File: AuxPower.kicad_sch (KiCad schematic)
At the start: 9 parts, among them U1 I6A4W020A033V-003-R

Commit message: Cleaning up for prototype run
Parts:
- added J1: Conn_01x02_Female, Connector_JST:JST_XH_B2B-XH-A_1x02_P2.50mm_Vertical, symbol Connector:Conn_01x02_Female
- RV1: MFN# (none) -> 3266W-1-503LF
- U1: MFN# (none) -> I6A24014A033V-003-R
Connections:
- net +9V: now also J1.1 (Pin_1)
- net GND: now also J1.2 (Pin_2)
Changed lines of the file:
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@@
   (junction (at 96.52 48.26) (diameter 0) (color 0 0 0 0)
   )
+  (junction (at 114.3 48.26) (diameter 0) (color 0 0 0 0)
+  )
   (junction (at 91.44 73.66) (diameter 0) (color 0 0 0 0)
   )
   (junction (at 101.6 55.88) (diameter 0) (color 0 0 0 0)
+  )
+  (junction (at 110.49 55.88) (diameter 0) (color 0 0 0 0)
   )
   (junction (at 26.67 55.88) (diameter 0) (color 0 0 0 0)
@@
     (stroke (width 0) (type default) (color 0 0 0 0))
   )
+  (wire (pts (xy 121.92 55.88) (xy 110.49 55.88))
+    (stroke (width 0) (type default) (color 0 0 0 0))
+  )
   (wire (pts (xy 101.6 55.88) (xy 110.49 55.88))
     (stroke (width 0) (type default) (color 0 0 0 0))
@@
     (stroke (width 0) (type default) (color 0 0 0 0))
   )
+  (wire (pts (xy 121.92 50.8) (xy 121.92 55.88))
+    (stroke (width 0) (type default) (color 0 0 0 0))
+  )
   (wire (pts (xy 52.07 53.34) (xy 52.07 48.26))
     (stroke (width 0) (type default) (color 0 0 0 0))
   )
   (wire (pts (xy 54.61 53.34) (xy 52.07 53.34))
+    (stroke (width 0) (type default) (color 0 0 0 0))
+  )
+  (wire (pts (xy 114.3 48.26) (xy 121.92 48.26))
     (stroke (width 0) (type default) (color 0 0 0 0))
   )
@@
     )
     (property "Datasheet" "~" (id 3) (at 45.72 53.34 0)
+      (effects (font (size 1.27 1.27)) hide)
+    )
+    (pin "1")
+    (pin "2")
+  )
+  (symbol (lib_id "Connector:Conn_01x02_Female") (at 127 48.26 0) (unit 1)
+    (in_bom yes) (on_board yes) (fields_autoplaced)
+    (property "Reference" "J1" (id 0) (at 128.27 49.5299 0)
+      (effects (font (size 1.27 1.27)) (justify left))
+    )
+    (property "Value" "Conn_01x02_Female" (id 1) (at 128.27 50.7999 0)
+      (effects (font (size 1.27 1.27)) (justify left) hide)
+    )
+    (property "Footprint" "Connector_JST:JST_XH_B2B-XH-A_1x02_P2.50mm_Vertical" (id 2) (at 127 48.26 0)
+      (effects (font (size 1.27 1.27)) hide)
+    )
+    (property "Datasheet" "~" (id 3) (at 127 48.26 0)
       (effects (font (size 1.27 1.27)) hide)
     )
@@
       (effects (font (size 1.27 1.27)) hide)
     )
-    (property "Datasheet" "~" (id 3) (at 97.79 73.66 0)
+    (property "Datasheet" "" (id 3) (at 97.79 73.66 0)
+      (effects (font (size 1.27 1.27)) hide)
+    )
+    (property "MFN#" "3266W-1-503LF" (id 4) (at 97.79 73.66 90)
       (effects (font (size 1.27 1.27)) hide)
     )
@@
       (effects (font (size 1.27 1.27)) hide)
     )
+    (property "MFN#" "I6A24014A033V-003-R" (id 4) (at 81.28 58.42 0)
+      (effects (font (size 1.27 1.27)) hide)
+    )

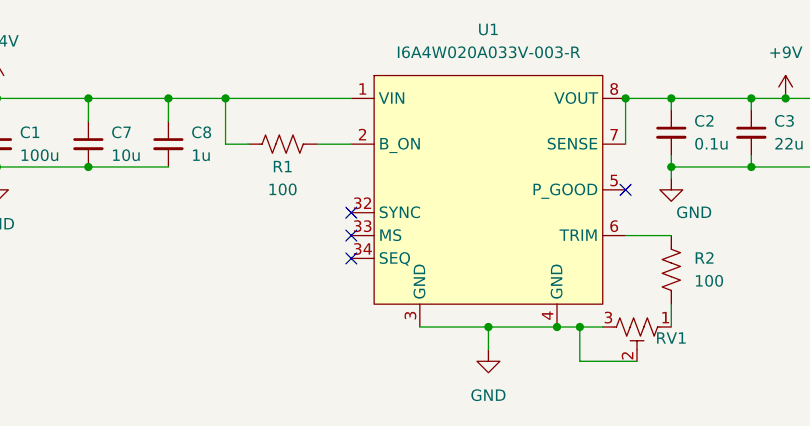
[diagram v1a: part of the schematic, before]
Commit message: No point using Fuses w/o fuse holders, Also added 3D models
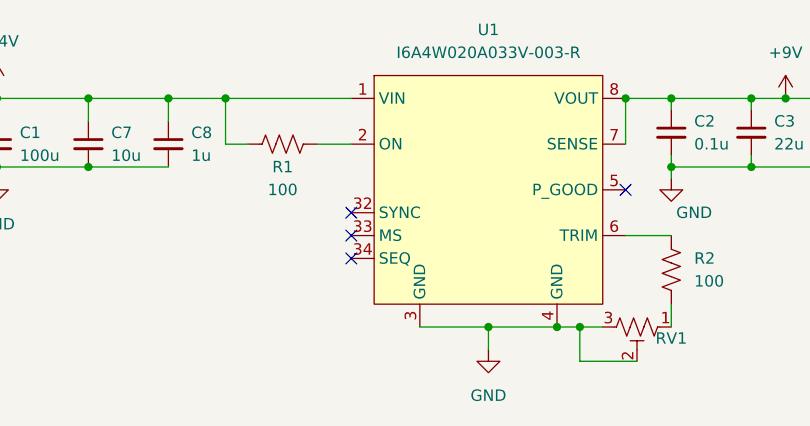
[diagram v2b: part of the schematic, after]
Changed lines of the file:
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@@
       (effects (font (size 1.27 1.27)) hide)
     )
+    (pin "1")
     (pin "2")
-    (pin "1")
     (pin "3")
     (pin "32")

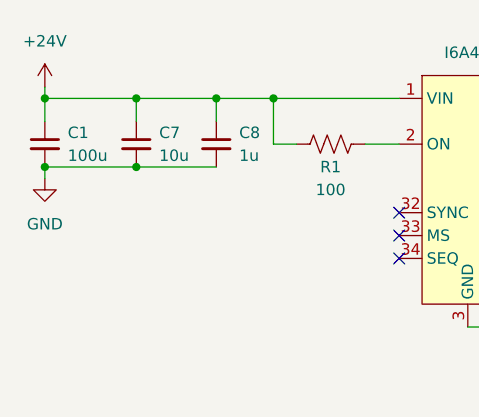
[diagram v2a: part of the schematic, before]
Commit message: Added BOM and updated Cap footprint according to availability
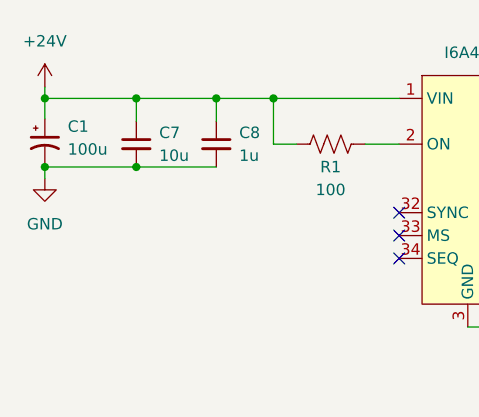
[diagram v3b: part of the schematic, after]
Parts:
- removed C1: 100u, Capacitor_SMD:C_0603_1608Metric, symbol Device:C_Small
- added C1: 100u, Capacitor_SMD:CP_Elec_10x10, symbol Device:C_Polarized_Small_US
- C3: footprint Capacitor_SMD:C_0603_1608Metric -> Capacitor_Tantalum_SMD:CP_EIA-7343-15_Kemet-W
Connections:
- net +24V: now also C1.1
- net GND: now also C1.2
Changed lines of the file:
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@@
   (junction (at 110.49 55.88) (diameter 0) (color 0 0 0 0)
   )
+  (junction (at 36.83 55.88) (diameter 0) (color 0 0 0 0)
+  )
+  (junction (at 26.67 48.26) (diameter 0) (color 0 0 0 0)
+  )
+  (junction (at 110.49 48.26) (diameter 0) (color 0 0 0 0)
+  )
+  (junction (at 36.83 48.26) (diameter 0) (color 0 0 0 0)
+  )
+  (junction (at 88.9 73.66) (diameter 0) (color 0 0 0 0)
+  )
+  (junction (at 81.28 73.66) (diameter 0) (color 0 0 0 0)
+  )
+  (junction (at 101.6 48.26) (diameter 0) (color 0 0 0 0)
+  )
+  (junction (at 52.07 48.26) (diameter 0) (color 0 0 0 0)
+  )
   (junction (at 26.67 55.88) (diameter 0) (color 0 0 0 0)
-  )
-  (junction (at 36.83 55.88) (diameter 0) (color 0 0 0 0)
-  )
-  (junction (at 26.67 48.26) (diameter 0) (color 0 0 0 0)
-  )
-  (junction (at 110.49 48.26) (diameter 0) (color 0 0 0 0)
-  )
-  (junction (at 36.83 48.26) (diameter 0) (color 0 0 0 0)
-  )
-  (junction (at 88.9 73.66) (diameter 0) (color 0 0 0 0)
-  )
-  (junction (at 81.28 73.66) (diameter 0) (color 0 0 0 0)
-  )
-  (junction (at 101.6 48.26) (diameter 0) (color 0 0 0 0)
-  )
-  (junction (at 52.07 48.26) (diameter 0) (color 0 0 0 0)
   )
   (junction (at 45.72 48.26) (diameter 0) (color 0 0 0 0)
@@
     (stroke (width 0) (type default) (color 0 0 0 0))
   )
-  (wire (pts (xy 26.67 48.26) (xy 26.67 50.8))
+  (wire (pts (xy 26.67 48.26) (xy 26.67 50.546))
+    (stroke (width 0) (type default) (color 0 0 0 0))
+  )
+  (wire (pts (xy 26.67 55.626) (xy 26.67 55.88))
+    (stroke (width 0) (type default) (color 0 0 0 0))
+  )
+  (wire (pts (xy 101.6 48.26) (xy 101.6 49.53))
+    (stroke (width 0) (type default) (color 0 0 0 0))
+  )
+  (wire (pts (xy 96.52 63.5) (xy 101.6 63.5))
+    (stroke (width 0) (type default) (color 0 0 0 0))
+  )
+  (wire (pts (xy 45.72 48.26) (xy 52.07 48.26))
+    (stroke (width 0) (type default) (color 0 0 0 0))
+  )
+  (wire (pts (xy 121.92 55.88) (xy 110.49 55.88))
+    (stroke (width 0) (type default) (color 0 0 0 0))
+  )
+  (wire (pts (xy 101.6 55.88) (xy 110.49 55.88))
+    (stroke (width 0) (type default) (color 0 0 0 0))
+  )
+  (wire (pts (xy 26.67 55.88) (xy 36.83 55.88))
+    (stroke (width 0) (type default) (color 0 0 0 0))
+  )
+  (wire (pts (xy 36.83 48.26) (xy 45.72 48.26))
+    (stroke (width 0) (type default) (color 0 0 0 0))
+  )
+  (wire (pts (xy 101.6 48.26) (xy 110.49 48.26))
+    (stroke (width 0) (type default) (color 0 0 0 0))
+  )
+  (wire (pts (xy 66.04 53.34) (xy 62.23 53.34))
+    (stroke (width 0) (type default) (color 0 0 0 0))
+  )
+  (wire (pts (xy 52.07 48.26) (xy 66.04 48.26))
+    (stroke (width 0) (type default) (color 0 0 0 0))
+  )
+  (wire (pts (xy 101.6 57.15) (xy 101.6 55.88))
+    (stroke (width 0) (type default) (color 0 0 0 0))
+  )
+  (wire (pts (xy 91.44 73.66) (xy 93.98 73.66))
+    (stroke (width 0) (type default) (color 0 0 0 0))
+  )
+  (wire (pts (xy 121.92 50.8) (xy 121.92 55.88))
+    (stroke (width 0) (type default) (color 0 0 0 0))
+  )
+  (wire (pts (xy 52.07 53.34) (xy 52.07 48.26))
+    (stroke (width 0) (type default) (color 0 0 0 0))
+  )
+  (wire (pts (xy 54.61 53.34) (xy 52.07 53.34))
     (stroke (width 0) (type default) (color 0 0 0 0))
   )
   (wire (pts (xy 26.67 55.88) (xy 26.67 57.15))
-    (stroke (width 0) (type default) (color 0 0 0 0))
-  )
-  (wire (pts (xy 101.6 48.26) (xy 101.6 49.53))
-    (stroke (width 0) (type default) (color 0 0 0 0))
-  )
-  (wire (pts (xy 96.52 63.5) (xy 101.6 63.5))
-    (stroke (width 0) (type default) (color 0 0 0 0))
-  )
-  (wire (pts (xy 45.72 48.26) (xy 52.07 48.26))
-    (stroke (width 0) (type default) (color 0 0 0 0))
-  )
-  (wire (pts (xy 121.92 55.88) (xy 110.49 55.88))
-    (stroke (width 0) (type default) (color 0 0 0 0))
-  )
-  (wire (pts (xy 101.6 55.88) (xy 110.49 55.88))
-    (stroke (width 0) (type default) (color 0 0 0 0))
-  )
-  (wire (pts (xy 26.67 55.88) (xy 36.83 55.88))
-    (stroke (width 0) (type default) (color 0 0 0 0))
-  )
-  (wire (pts (xy 36.83 48.26) (xy 45.72 48.26))
-    (stroke (width 0) (type default) (color 0 0 0 0))
-  )
-  (wire (pts (xy 101.6 48.26) (xy 110.49 48.26))
-    (stroke (width 0) (type default) (color 0 0 0 0))
-  )
-  (wire (pts (xy 66.04 53.34) (xy 62.23 53.34))
-    (stroke (width 0) (type default) (color 0 0 0 0))
-  )
-  (wire (pts (xy 52.07 48.26) (xy 66.04 48.26))
-    (stroke (width 0) (type default) (color 0 0 0 0))
-  )
-  (wire (pts (xy 101.6 57.15) (xy 101.6 55.88))
-    (stroke (width 0) (type default) (color 0 0 0 0))
-  )
-  (wire (pts (xy 91.44 73.66) (xy 93.98 73.66))
-    (stroke (width 0) (type default) (color 0 0 0 0))
-  )
-  (wire (pts (xy 121.92 50.8) (xy 121.92 55.88))
-    (stroke (width 0) (type default) (color 0 0 0 0))
-  )
-  (wire (pts (xy 52.07 53.34) (xy 52.07 48.26))
-    (stroke (width 0) (type default) (color 0 0 0 0))
-  )
-  (wire (pts (xy 54.61 53.34) (xy 52.07 53.34))
     (stroke (width 0) (type default) (color 0 0 0 0))
   )
@@
       (effects (font (size 1.27 1.27)) (justify left))
     )
-    (property "Footprint" "Capacitor_SMD:C_0603_1608Metric" (id 2) (at 110.49 52.07 0)
+    (property "Footprint" "Capacitor_Tantalum_SMD:CP_EIA-7343-15_Kemet-W" (id 2) (at 110.49 52.07 0)
       (effects (font (size 1.27 1.27)) hide)
     )
@@
     )
     (property "Datasheet" "~" (id 3) (at 127 48.26 0)
-      (effects (font (size 1.27 1.27)) hide)
-    )
-    (pin "1")
-    (pin "2")
-  )
-  (symbol (lib_id "Device:C_Small") (at 26.67 53.34 0) (unit 1)
-    (in_bom yes) (on_board yes) (fields_autoplaced)
-    (property "Reference" "C1" (id 0) (at 29.21 52.0762 0)
-      (effects (font (size 1.27 1.27)) (justify left))
-    )
-    (property "Value" "100u" (id 1) (at 29.21 54.6162 0)
-      (effects (font (size 1.27 1.27)) (justify left))
-    )
-    (property "Footprint" "Capacitor_SMD:C_0603_1608Metric" (id 2) (at 26.67 53.34 0)
-      (effects (font (size 1.27 1.27)) hide)
-    )
-    (property "Datasheet" "~" (id 3) (at 26.67 53.34 0)
       (effects (font (size 1.27 1.27)) hide)
     )
@@
     (pin "1")
   )
+  (symbol (lib_id "Device:C_Polarized_Small_US") (at 26.67 53.086 0) (unit 1)
+    (in_bom yes) (on_board yes) (fields_autoplaced)
+    (property "Reference" "C1" (id 0) (at 29.21 51.3841 0)
+      (effects (font (size 1.27 1.27)) (justify left))
+    )
+    (property "Value" "100u" (id 1) (at 29.21 53.9241 0)
+      (effects (font (size 1.27 1.27)) (justify left))
+    )
+    (property "Footprint" "Capacitor_SMD:CP_Elec_10x10" (id 2) (at 26.67 53.086 0)
+      (effects (font (size 1.27 1.27)) hide)
+    )
+    (property "Datasheet" "~" (id 3) (at 26.67 53.086 0)
+      (effects (font (size 1.27 1.27)) hide)
+    )
+    (pin "1")
+    (pin "2")
+  )
 )

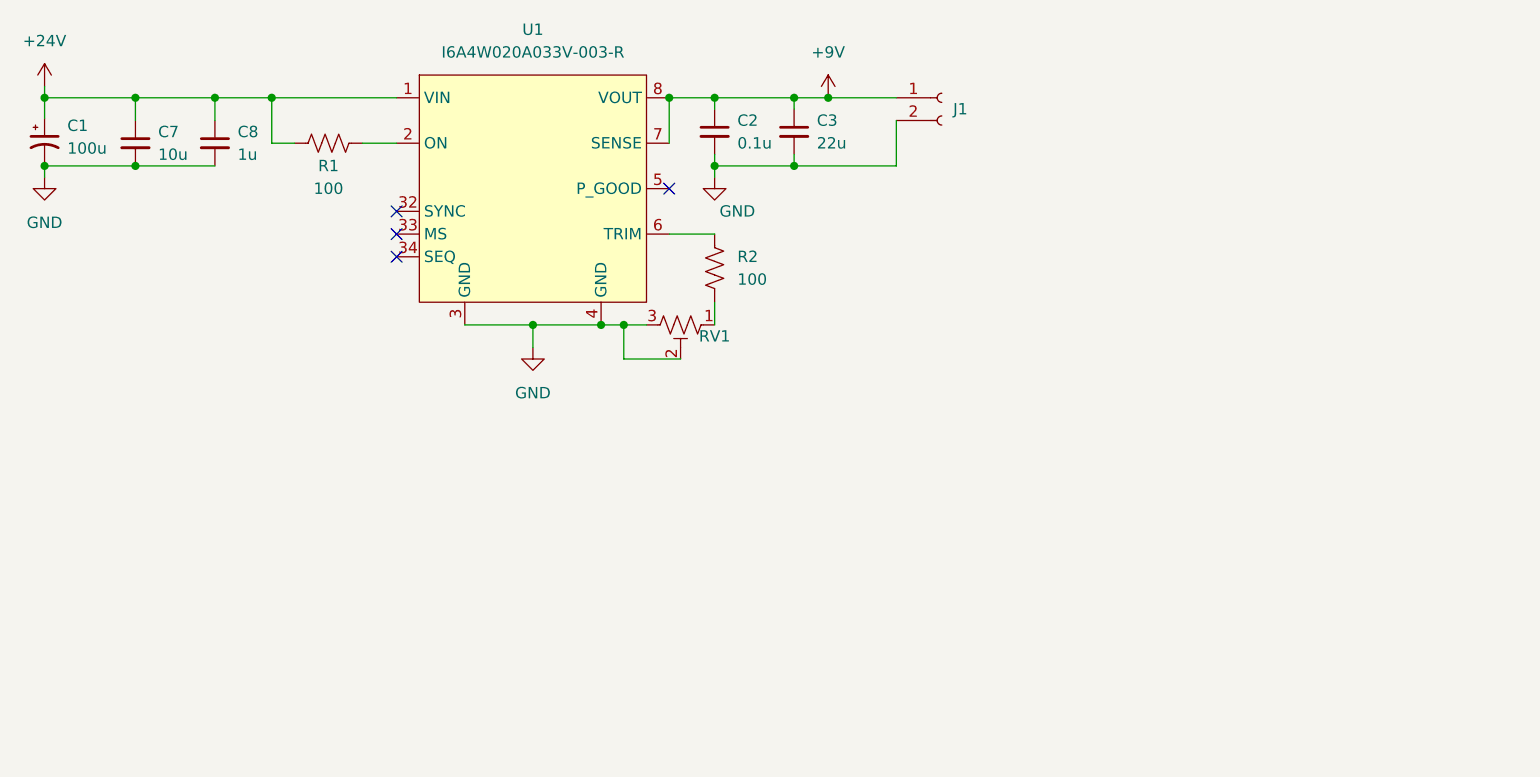
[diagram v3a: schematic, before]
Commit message: Changed resistors and LEDs to 0805 and updated Production files
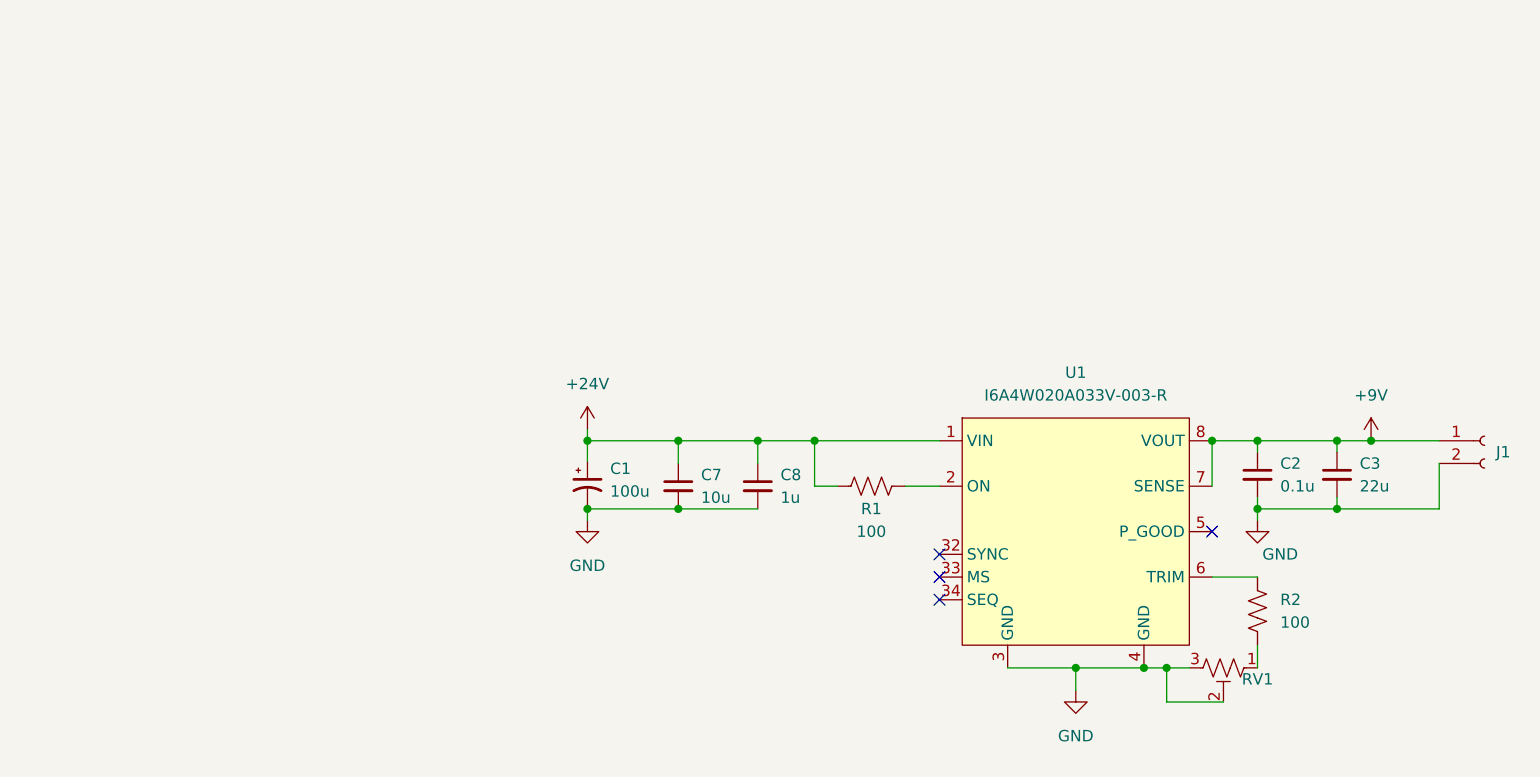
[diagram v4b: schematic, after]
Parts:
- R1, R2: footprint Resistor_SMD:R_0603_1608Metric -> Resistor_SMD:R_0805_2012Metric
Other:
- moved on the sheet: C1, C2, C3, C7, C8, J1, R1, R2, RV1, U1
